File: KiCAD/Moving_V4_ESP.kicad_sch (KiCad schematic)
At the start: 46 parts, among them J1 Vin_1, J2 Vin_2, J3 Power_SW, J4 USB_B_Micro, J5 MOTOR_R, J6 Motor_L, SW1 SW_Reset, U1 CH340X, U2 UZ1085L-33-TN3-R, U3 ESP32-WROOM-32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

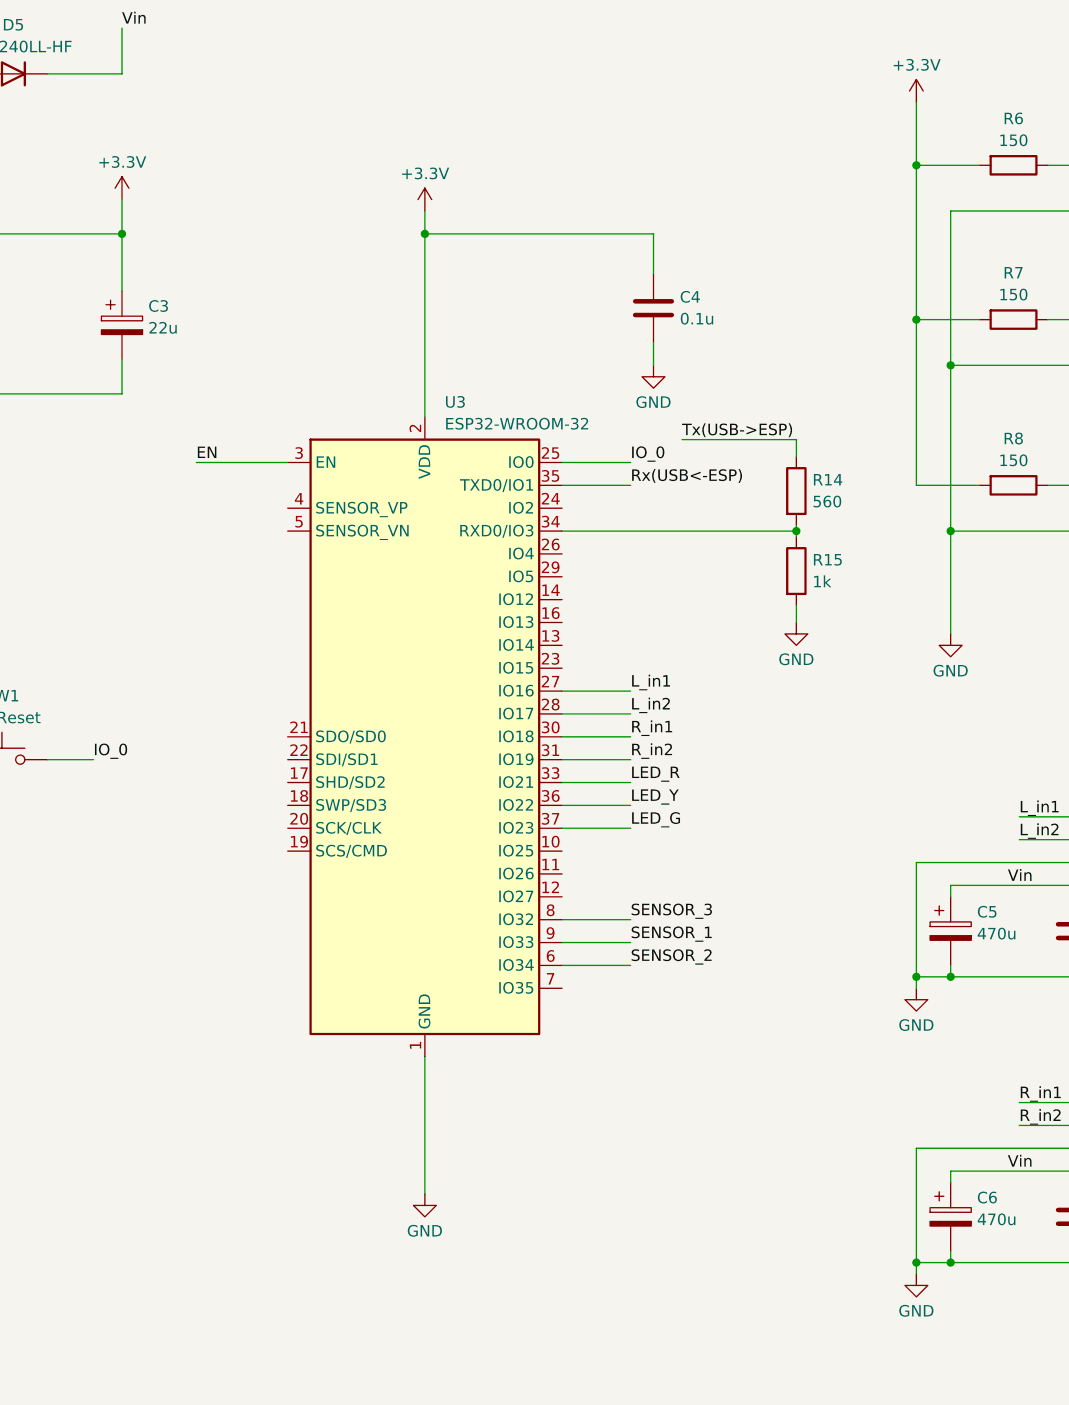
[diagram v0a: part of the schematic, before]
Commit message: UART分圧抵抗にコンデンサを追加
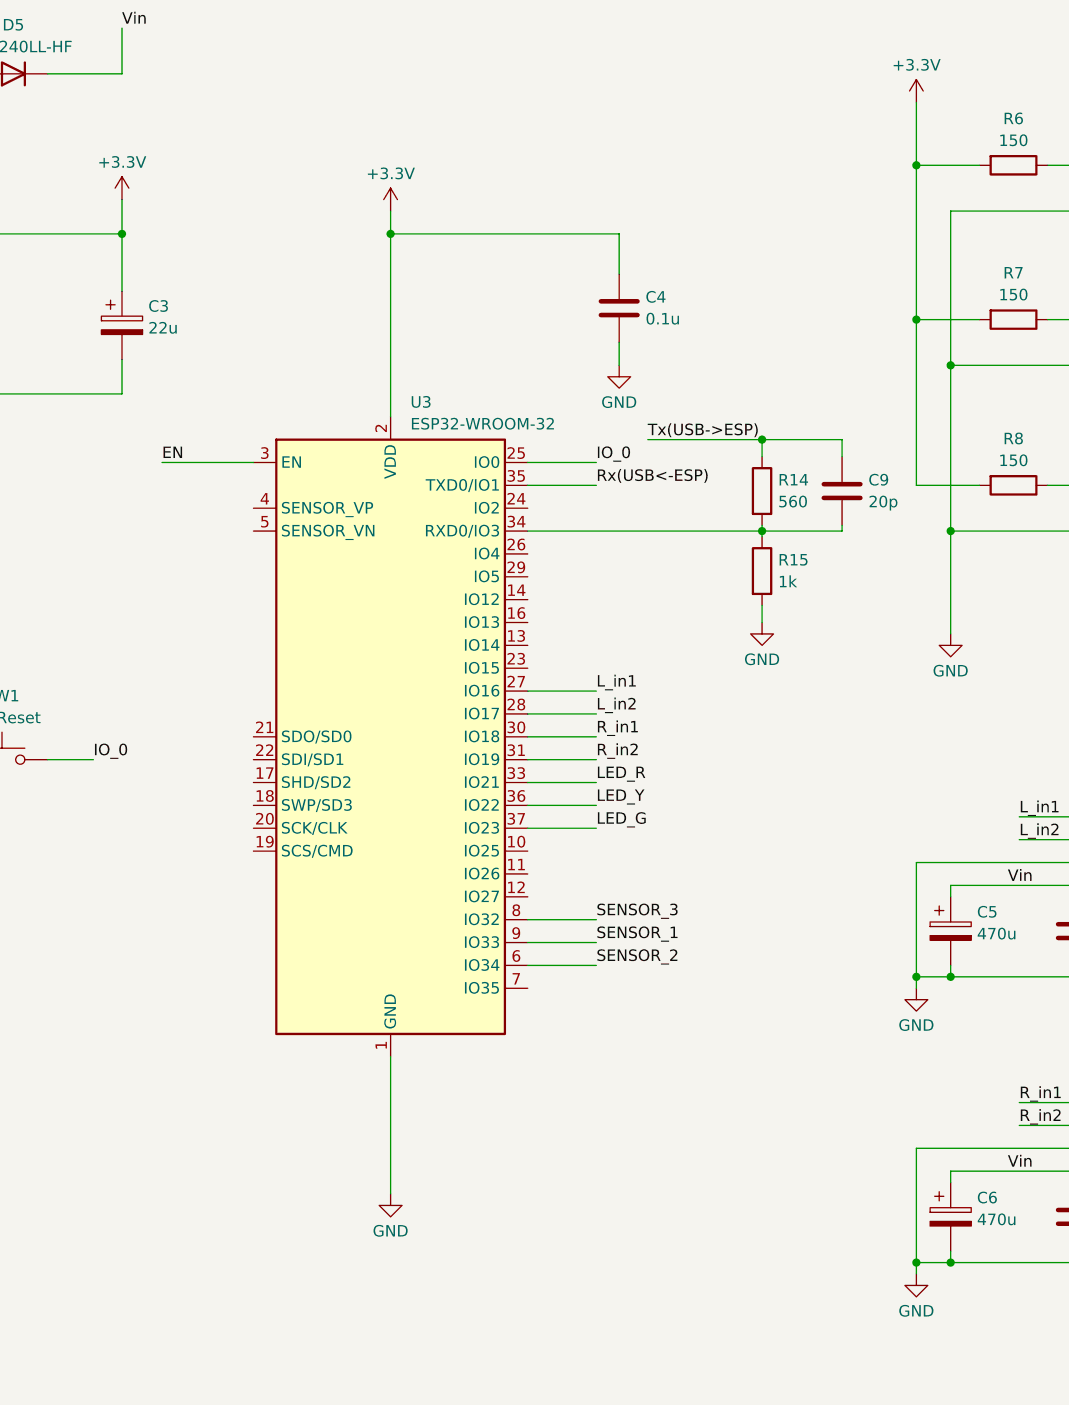
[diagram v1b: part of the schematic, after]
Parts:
- added C9: 20p, Capacitor_SMD:C_0402_1005Metric, symbol Device:C
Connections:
- net Tx(USB->ESP): now also C9.1
- net at R14.2, R15.1, U3.34 (RXD0/IO3): now also C9.2
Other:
- moved on the sheet: C4, R14, R15, U3

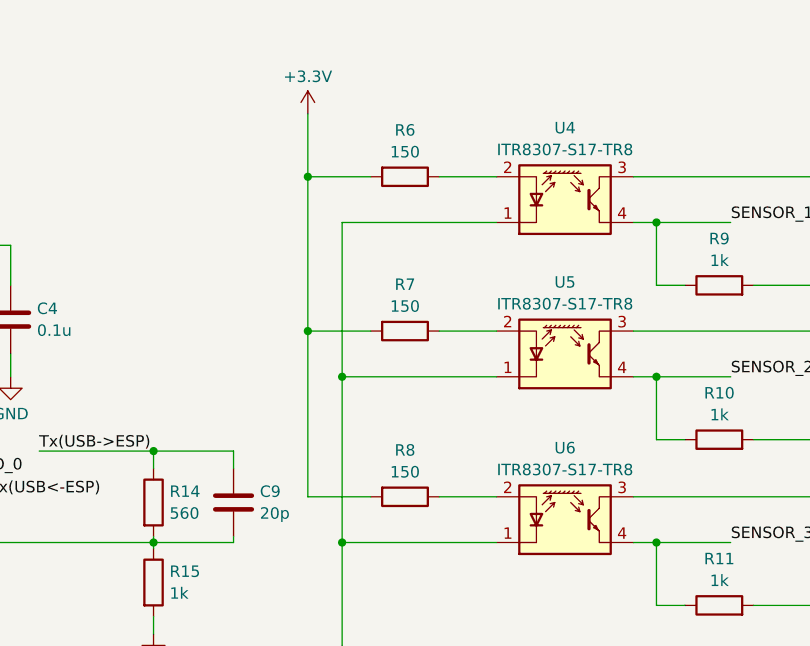
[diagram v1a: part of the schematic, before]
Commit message: フォトリフレクタのLED電流制限抵抗を50Ωに変更
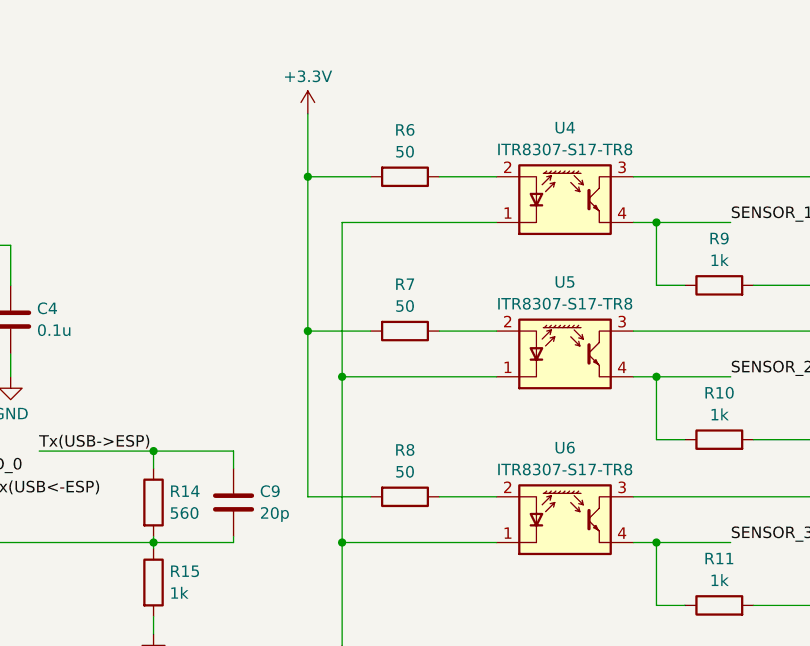
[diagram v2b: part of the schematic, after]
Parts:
- R6, R7, R8: value 150 -> 50; footprint Resistor_SMD:R_0402_1005Metric -> Resistor_SMD:R_0805_2012Metric; LCSC C159952 -> C2828866
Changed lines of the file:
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@@
+    )
+  )
+  (symbol (lib_id "Device:R") (at 224.155 50.165 270) (unit 1)
+    (in_bom yes) (on_board yes) (dnp no) (fields_autoplaced)
+    (property "Reference" "R7" (at 224.155 45.0047 90)
+      (effects (font (size 1.27 1.27)))
+    )
+    (property "Value" "50" (at 224.155 47.4289 90)
+      (effects (font (size 1.27 1.27)))
+    )
+    (property "Footprint" "Resistor_SMD:R_0805_2012Metric" (at 224.155 48.387 90)
+      (effects (font (size 1.27 1.27)) hide)
+    )
+    (property "Datasheet" "~" (at 224.155 50.165 0)
+      (effects (font (size 1.27 1.27)) hide)
+    )
+    (property "LCSC" "C2828866" (at 224.155 50.165 0)
+      (effects (font (size 1.27 1.27)) hide)
+    )
+    (pin "1")
+    (pin "2")
+    (instances
+      (project "Moving_V4_ESP"
+        (path "/515135d2-db88-48ff-b508-cbebeed2b019"
+          (reference "R7") (unit 1)
+        )
+      )
     )
   )
@@
       (effects (font (size 1.27 1.27)))
     )
-    (property "Value" "150" (at 224.155 30.2839 90)
-      (effects (font (size 1.27 1.27)))
-    )
-    (property "Footprint" "Resistor_SMD:R_0402_1005Metric" (at 224.155 31.242 90)
+    (property "Value" "50" (at 224.155 30.2839 90)
+      (effects (font (size 1.27 1.27)))
+    )
+    (property "Footprint" "Resistor_SMD:R_0805_2012Metric" (at 224.155 31.242 90)
       (effects (font (size 1.27 1.27)) hide)
     )
@@
       (effects (font (size 1.27 1.27)) hide)
     )
-    (property "LCSC" "C159952" (at 224.155 33.02 0)
+    (property "LCSC" "C2828866" (at 224.155 33.02 0)
       (effects (font (size 1.27 1.27)) hide)
     )
@@
         (path "/515135d2-db88-48ff-b508-cbebeed2b019"
           (reference "R11") (unit 1)
-        )
-      )
-    )
-  )
-  (symbol (lib_id "Device:R") (at 224.155 68.58 270) (unit 1)
-    (in_bom yes) (on_board yes) (dnp no) (fields_autoplaced)
-    (property "Reference" "R8" (at 224.155 63.4197 90)
-      (effects (font (size 1.27 1.27)))
-    )
-    (property "Value" "150" (at 224.155 65.8439 90)
-      (effects (font (size 1.27 1.27)))
-    )
-    (property "Footprint" "Resistor_SMD:R_0402_1005Metric" (at 224.155 66.802 90)
-      (effects (font (size 1.27 1.27)) hide)
-    )
-    (property "Datasheet" "~" (at 224.155 68.58 0)
-      (effects (font (size 1.27 1.27)) hide)
-    )
-    (property "LCSC" "C159952" (at 224.155 68.58 0)
-      (effects (font (size 1.27 1.27)) hide)
-    )
-    (pin "1")
-    (pin "2")
-    (instances
-      (project "Moving_V4_ESP"
-        (path "/515135d2-db88-48ff-b508-cbebeed2b019"
-          (reference "R8") (unit 1)
         )
       )
@@
     )
   )
+  (symbol (lib_id "Device:R") (at 224.155 68.58 270) (unit 1)
+    (in_bom yes) (on_board yes) (dnp no) (fields_autoplaced)
+    (property "Reference" "R8" (at 224.155 63.4197 90)
+      (effects (font (size 1.27 1.27)))
+    )
+    (property "Value" "50" (at 224.155 65.8439 90)
+      (effects (font (size 1.27 1.27)))
+    )
+    (property "Footprint" "Resistor_SMD:R_0805_2012Metric" (at 224.155 66.802 90)
+      (effects (font (size 1.27 1.27)) hide)
+    )
+    (property "Datasheet" "~" (at 224.155 68.58 0)
+      (effects (font (size 1.27 1.27)) hide)
+    )
+    (property "LCSC" "C2828866" (at 224.155 68.58 0)
+      (effects (font (size 1.27 1.27)) hide)
+    )
+    (pin "1")
+    (pin "2")
+    (instances
+      (project "Moving_V4_ESP"
+        (path "/515135d2-db88-48ff-b508-cbebeed2b019"
+          (reference "R8") (unit 1)
+        )
+      )
+    )
+  )
   (symbol (lib_id "Device:LED") (at 26.67 172.72 90) (unit 1)
     (in_bom yes) (on_board yes) (dnp no) (fields_autoplaced)
@@
         )
       )
-    )
-  )
-  (symbol (lib_id "Device:R") (at 224.155 50.165 270) (unit 1)
-    (in_bom yes) (on_board yes) (dnp no) (fields_autoplaced)
-    (property "Reference" "R7" (at 224.155 45.0047 90)
-      (effects (font (size 1.27 1.27)))
-    )
-    (property "Value" "150" (at 224.155 47.4289 90)
-      (effects (font (size 1.27 1.27)))
-    )
-    (property "Footprint" "Resistor_SMD:R_0402_1005Metric" (at 224.155 48.387 90)
-      (effects (font (size 1.27 1.27)) hide)
-    )
-    (property "Datasheet" "~" (at 224.155 50.165 0)
-      (effects (font (size 1.27 1.27)) hide)
-    )
-    (property "LCSC" "C159952" (at 224.155 50.165 0)
-      (effects (font (size 1.27 1.27)) hide)
-    )
-    (pin "1")
-    (pin "2")
-    (instances
-      (project "Moving_V4_ESP"
-        (path "/515135d2-db88-48ff-b508-cbebeed2b019"
-          (reference "R7") (unit 1)
-        )
-      )

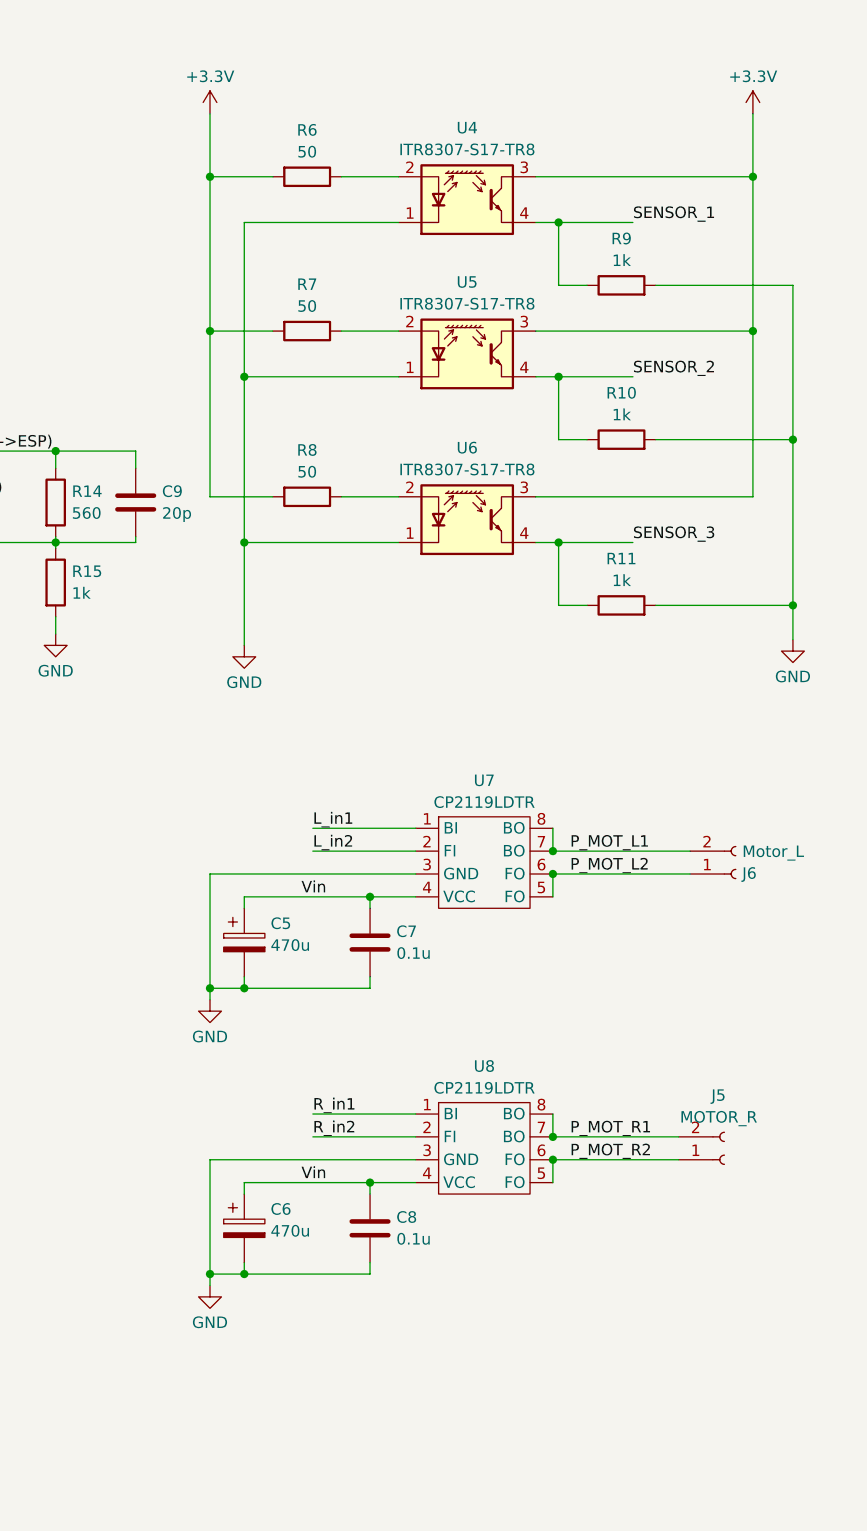
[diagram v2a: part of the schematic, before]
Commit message: フォトリフレクタをジャンパで選択できるように変更
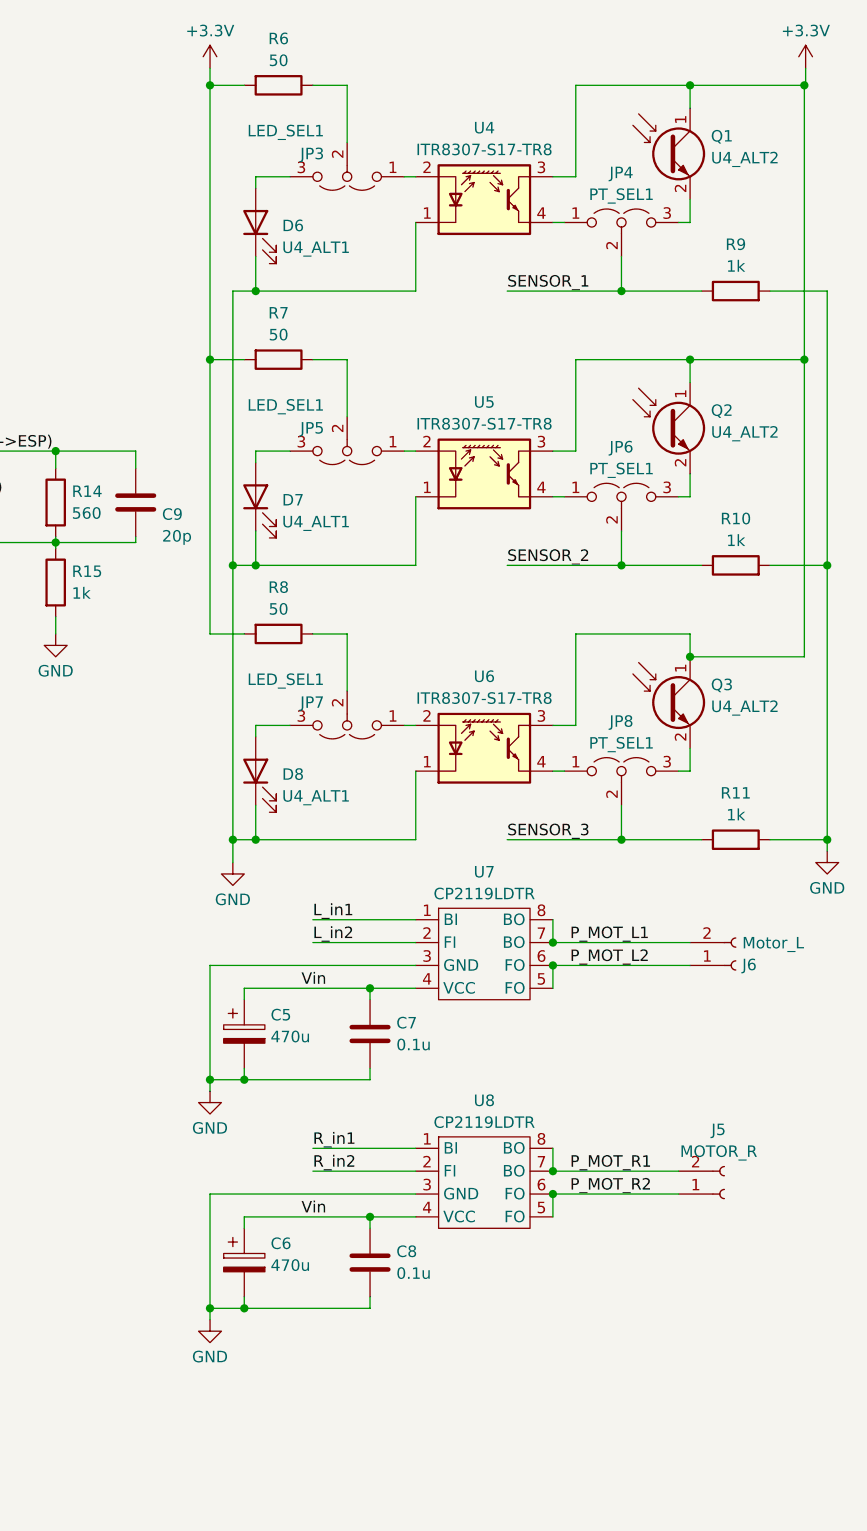
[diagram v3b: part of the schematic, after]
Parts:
- added D6, D7, D8: U4_ALT1, LED_THT:LED_D5.0mm, symbol Device:LED
- added JP3, JP5, JP7: LED_SEL1, Jumper:SolderJumper-3_P1.3mm_Open_RoundedPad1.0x1.5mm, symbol Jumper:Jumper_3_Open
- added JP4, JP6, JP8: PT_SEL1, Jumper:SolderJumper-3_P1.3mm_Open_RoundedPad1.0x1.5mm, symbol Jumper:Jumper_3_Open
- added Q1, Q2, Q3: U4_ALT2, LED_THT:LED_D5.0mm, symbol Device:Q_Photo_NPN
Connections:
- net +3.3V: now also Q1.1 (C), Q2.1 (C), Q3.1 (C)
- net GND: now also D6.1 (K), D7.1 (K), D8.1 (K)
- net SENSOR_1: now also JP4.2 (C); no longer U4.4
- net SENSOR_2: now also JP6.2 (C); no longer U5.4
- net SENSOR_3: now also JP8.2 (C); no longer U6.4
- net at U5.2 (A): now also JP5.1 (A); no longer R7.1
- net at R6.1: now also JP3.2 (C); no longer U4.2 (A)
- net at U6.2 (A): now also JP7.1 (A); no longer R8.1
- new net: D7.2 (A), JP5.3 (B)
- new net: D8.2 (A), JP7.3 (B)
- new net: D6.2 (A), JP3.3 (B)
- new net: JP4.1 (A), U4.4
- new net: JP4.3 (B), Q1.2 (E)
- new net: JP6.1 (A), U5.4
- new net: JP6.3 (B), Q2.2 (E)
- new net: JP8.3 (B), Q3.2 (E)
- new net: JP5.2 (C), R7.1
- new net: JP8.1 (A), U6.4
- new net: JP7.2 (C), R8.1
- new net: JP3.1 (A), U4.2 (A)
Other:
- moved on the sheet: C5, C6, C7, C8, J5, J6, R6, R9, U4, U7, U8
